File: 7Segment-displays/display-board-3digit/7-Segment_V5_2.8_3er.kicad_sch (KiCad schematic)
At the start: 4 parts, among them J1 Conn_02x08_Odd_Even, U1 7Segment 3 digit common catho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

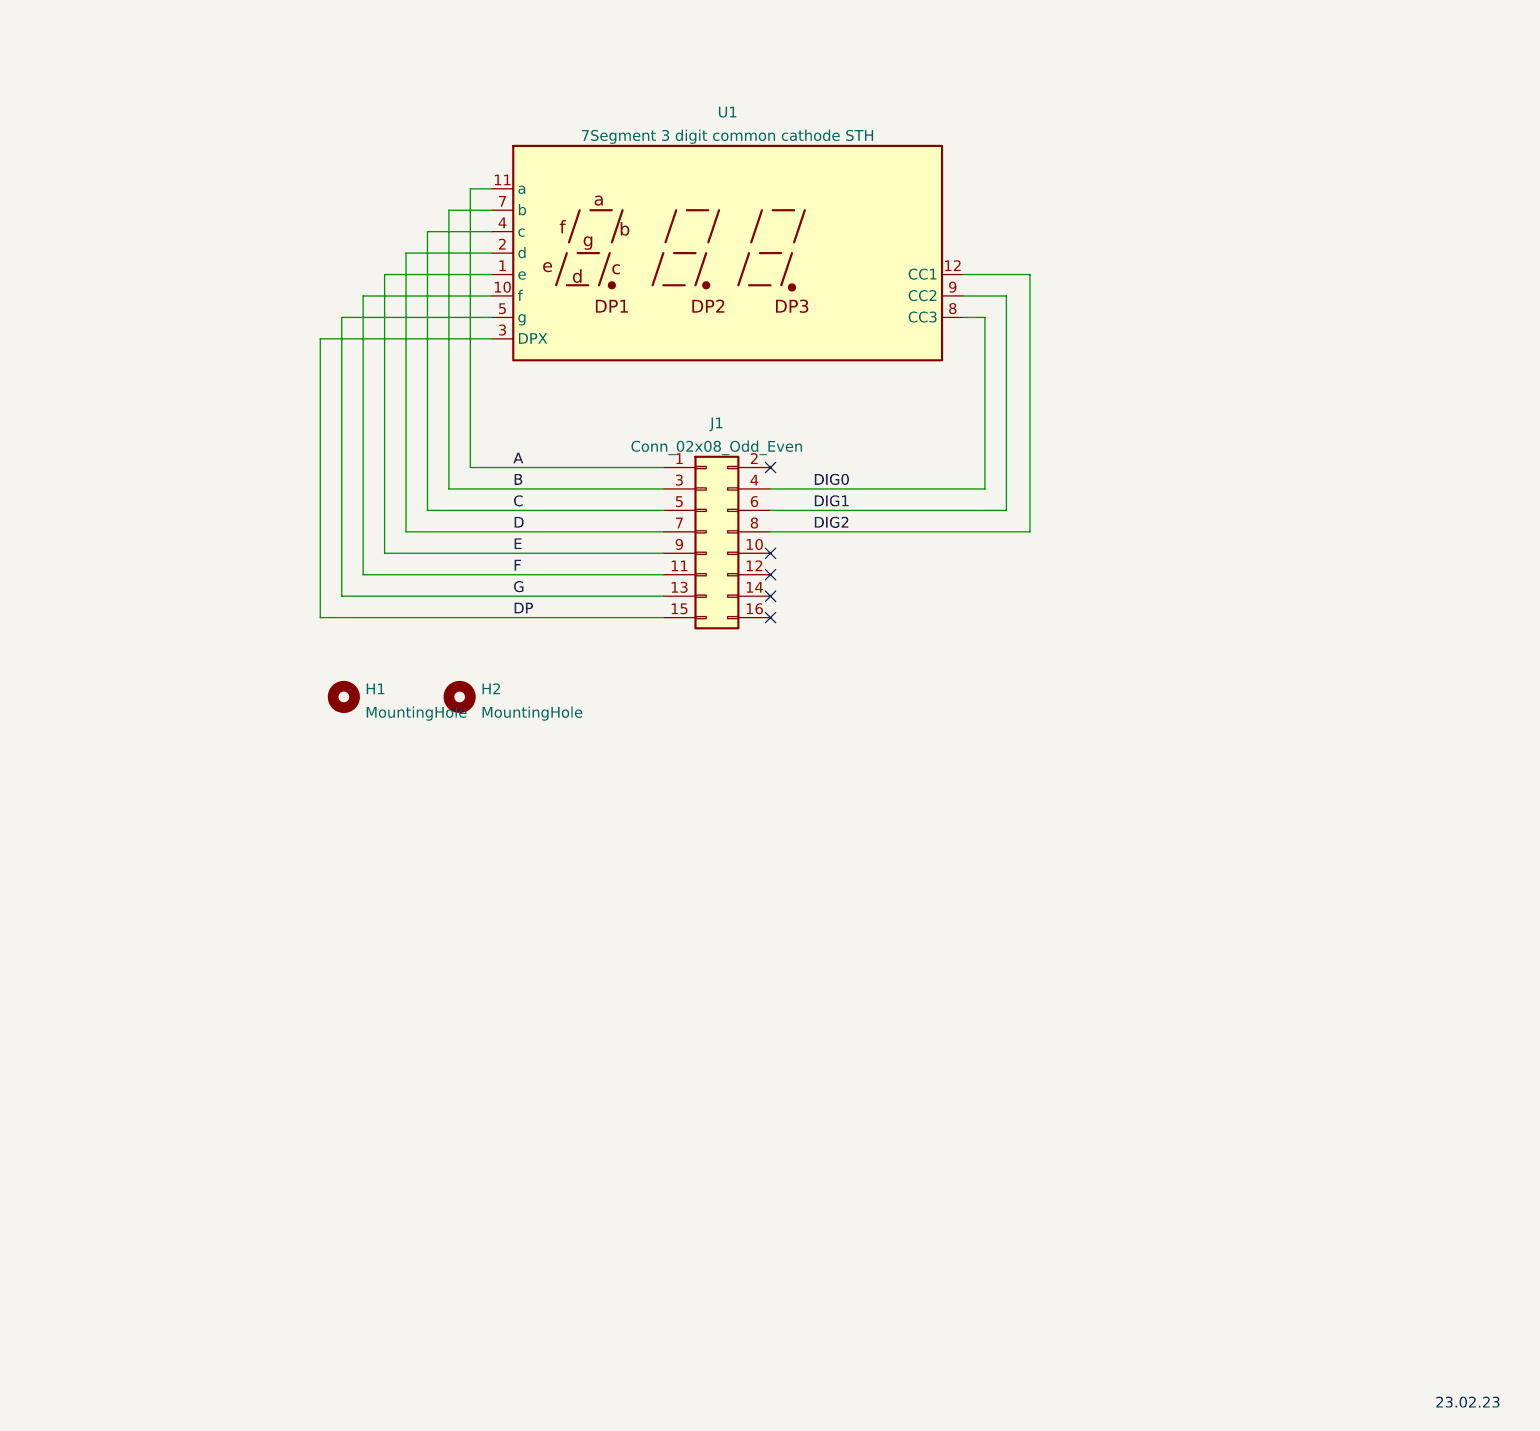
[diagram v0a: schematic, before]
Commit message: update 4/5/6 digit schematic and pcb to MF lib, add 3 digit to lib
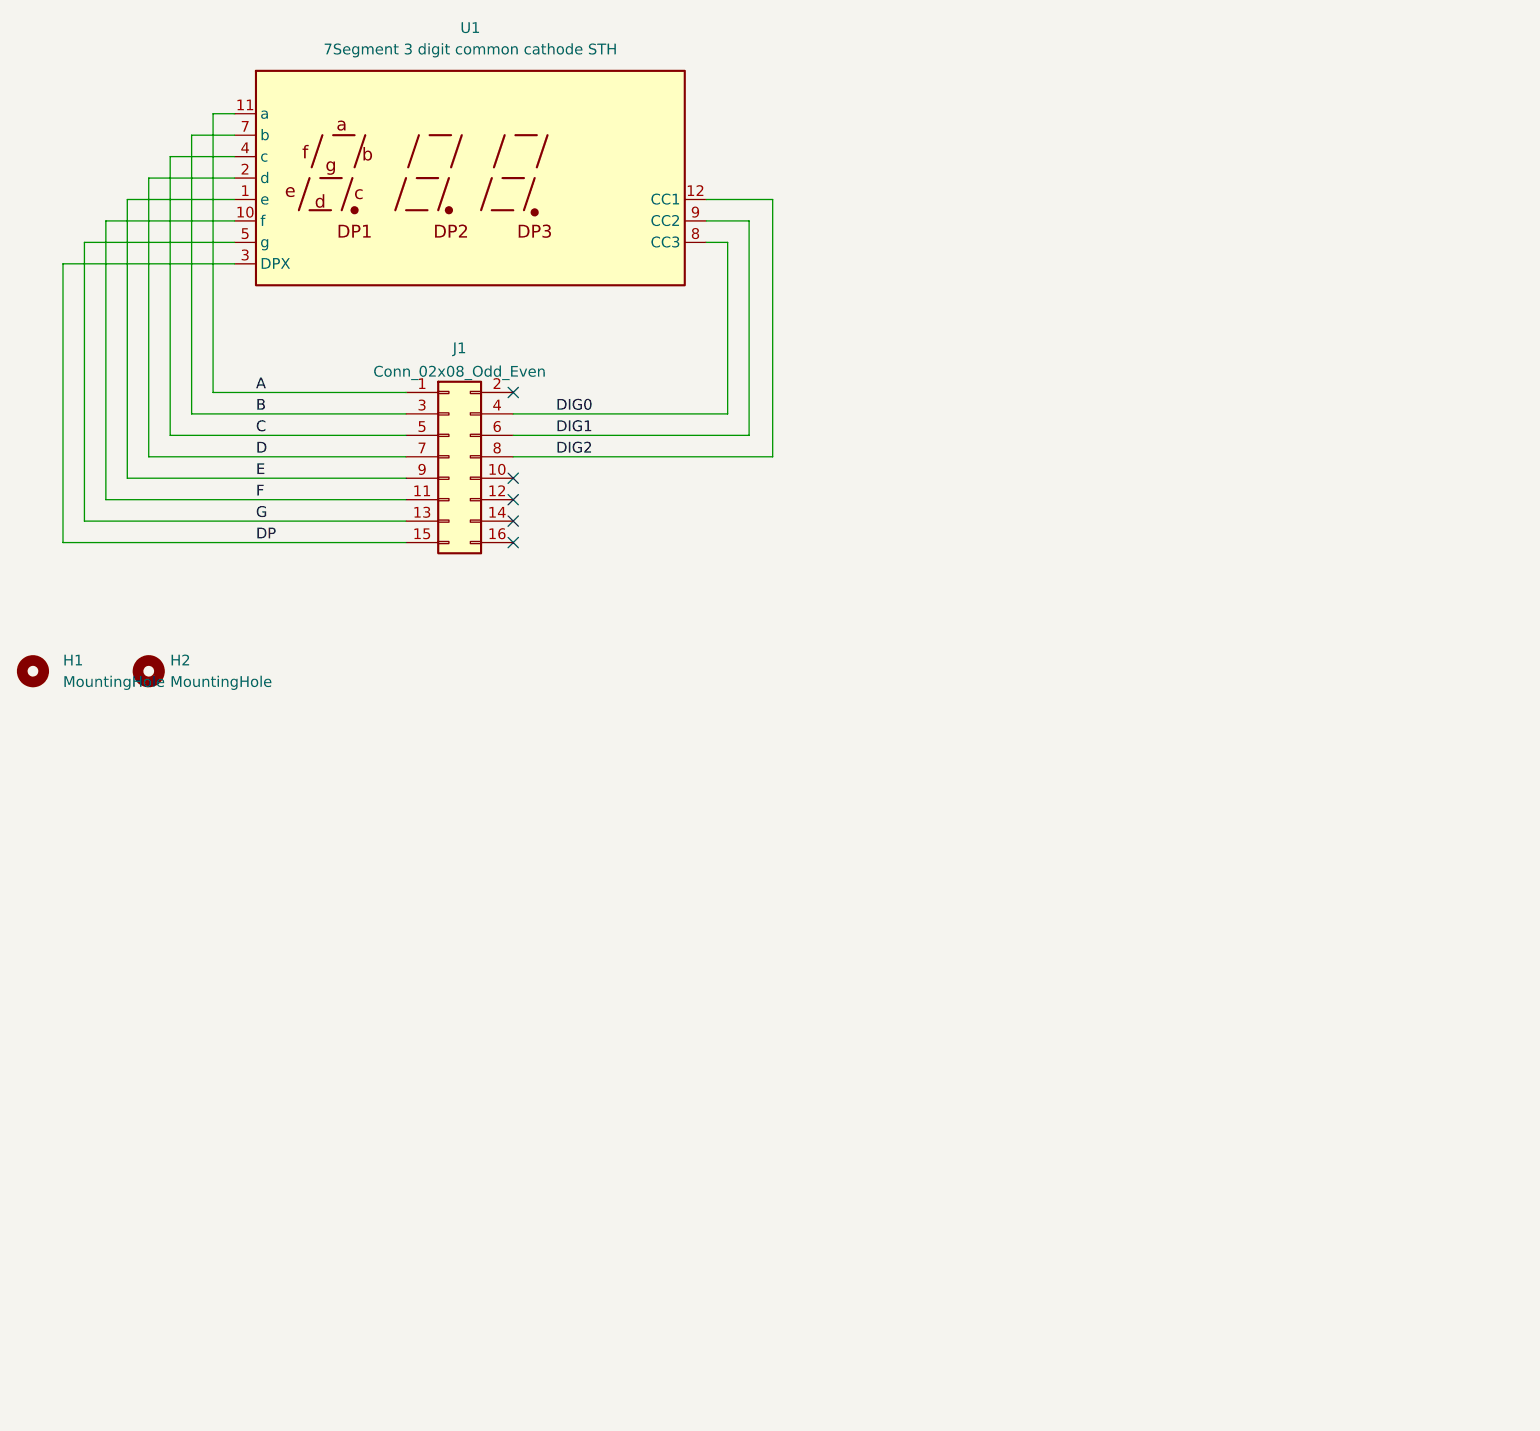
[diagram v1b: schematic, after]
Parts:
- H1, H2: footprint (none) -> MountingHole:MountingHole_3.2mm_M3_Pad; symbol Mechanical:MountingHole -> MobiFlight:MountingHole 3.2mm; now left out of the parts list
- U1: footprint Display_7Segment:STH_7_3 Digits_0.28_CC -> MobiFlight:STH_7_3 Digits_0.28_CC; symbol Display_Character:7Segment 3 digit common cathode STH -> MobiFlight:7Segment 3 digit common cathode STH
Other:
- note removed: "23.02.23"
- company: (none) -> MobiFlight
- title: (none) -> 7 Segment Display Module, 3 digits
- moved on the sheet: H1, H2, J1, U1
